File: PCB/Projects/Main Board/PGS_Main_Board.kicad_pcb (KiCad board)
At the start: 4 copper layers, 109.5 x 60.7 mm, 120 parts, among them J1 SM02B-SURS-TF_LF__SN_, J11 Molex 505110-0592, J2 SM02B-SURS-TF_LF__SN_, J3 Molex 505110-0892, J5 Molex 505110-0892, J7 Molex 505110-0452, J8 Conn_01x04_Pin, J9 Molex 505110-1792, Q1 MMBT2222A, Q2 MMBT2222A, SW10 SW_Push, SW11 SW_Push, SW3 SW_Push, SW4 SW_Push, SW5 SW_Push, SW6 SW_Push, SW7 SW_Push, SW8 SW_Push, SW9 SW_Push, U1 HAL4395, U10 HAL4395, U11 HAL4395, U2 RP2350_80QFN, U3 HAL4395, U4 ST_LSM6, U5 ST_LSM6, U6 HAL4395, U7 HAL4395, U8 HAL4395, U9 HAL4395, Y1 ABM8-272-T3

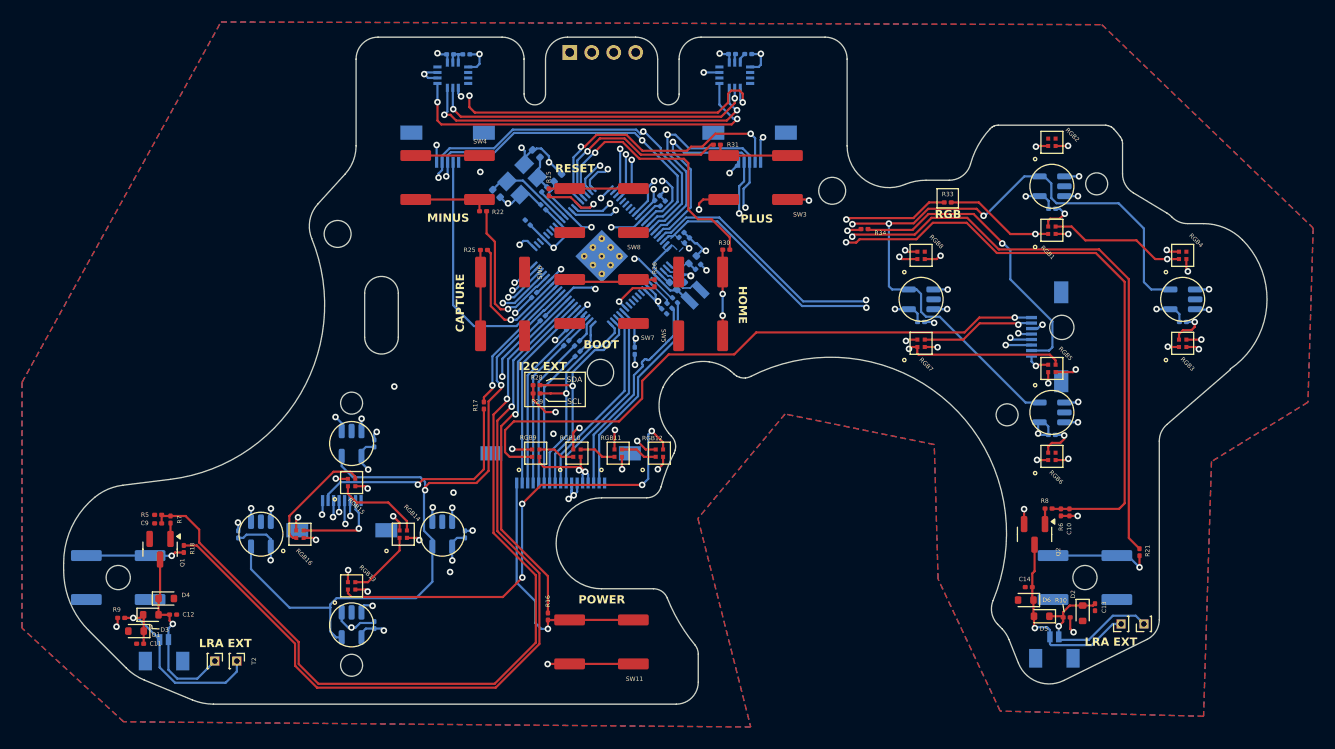
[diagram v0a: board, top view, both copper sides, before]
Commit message: Sync local board work; replace Trigger Board with Trigger FPC
- Update Main, Stick and USBW board layouts, schematics and 3D exports
- Replace the rigid Trigger Board project with the new Trigger FPC design
- Add shared PCB/Libraries footprint library and fp-lib-table
- Regenerate production outputs (gerbers, drills, placement, BOM) for all boards
- Stop tracking KiCad auto-backup folders and fp-info-cache; consolidate .gitignore

Co-Authored-By: Claude Opus 5 <noreply@anthropic.com>
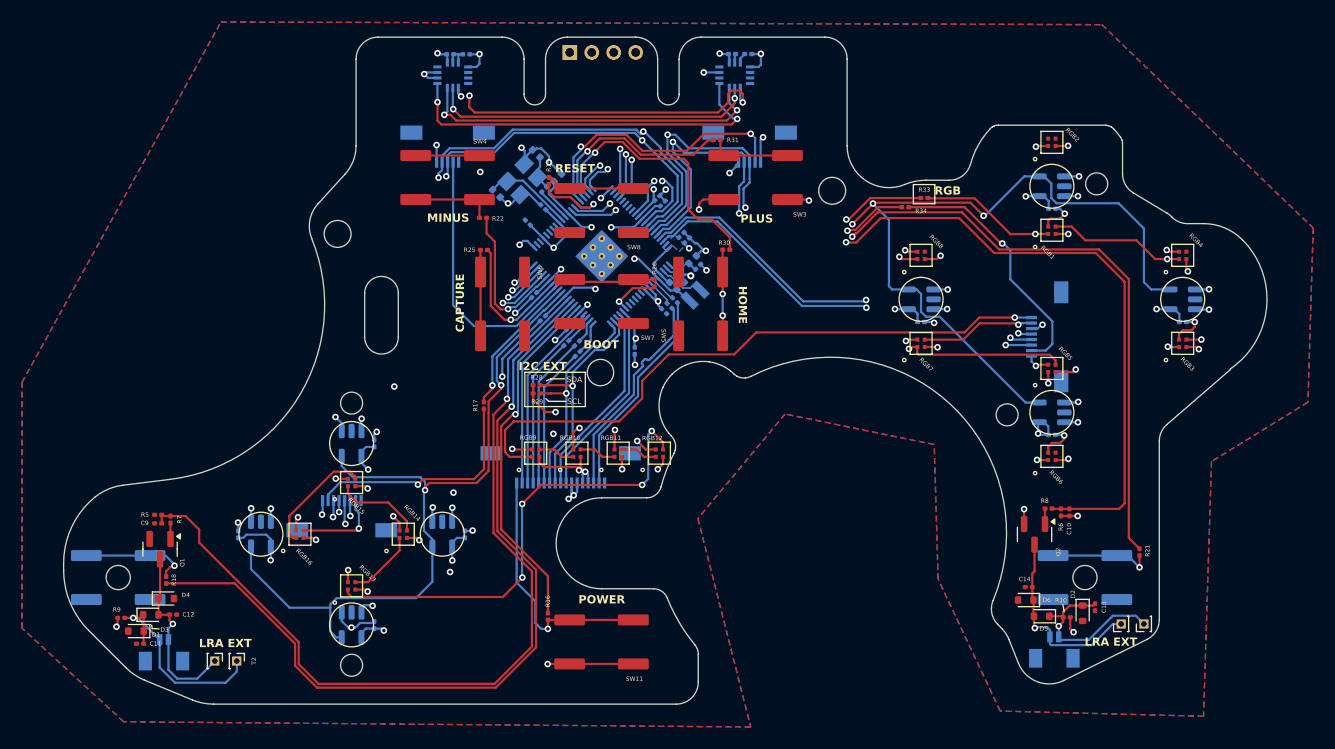
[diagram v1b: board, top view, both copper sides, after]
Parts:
- moved R34 4.20 mm to (98.4, 28.8)
- moved R18 3.24 mm to (31.2, 62.8), turned to -90 degrees
- moved R33 2.16 mm to (100.2, 28.0)
- moved R15 1.02 mm to (66.0, 26.5)
- moved R22 0.60 mm to (60.0, 29.8)
- moved R31 0.42 mm to (81.3, 22.7)
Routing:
- net Net-(U2-GPIO33): track 30.8 -> 35.3 mm
- net STICK_R_BTN_IN: track 27.4 -> 23.1 mm
- net ABXY_EN: track 92.6 -> 95.5 mm
- net RGB_OUT: track 19.1 -> 21.4 mm
- net Net-(U2-GPIO35): track 36.2 -> 34.3 mm
- net GRIP_L_BTN: track 9.00 -> 9.92 mm
- net Net-(U2-RUN): track 6.36 -> 7.15 mm
- net MINUS_BTN: track 6.87 -> 7.47 mm
- net Net-(U2-GPIO16): track 14.8 -> 14.2 mm
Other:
- outline, holes or cut-outs redrawn
